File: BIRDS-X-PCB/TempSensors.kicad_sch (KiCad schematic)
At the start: 10 parts, among them U307 STDS75DS2F, U312 STDS75DS2F, U313 STDS75DS2F, U314 STDS75DS2F, U315 STDS75DS2F

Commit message: Prep docs for Rev5.1 release
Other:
- note added: "Note: Rev5 and Rev5.1 are missing I2C pull-up resistors. I2C pull-up resistors will be added in next rev."
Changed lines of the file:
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@@
   (paper "A4")
   (title_block
-    (rev "Rev5.0")
+    (date "2023-09-07")
+    (rev "Rev5.1")
   )
   (junction (at 92.71 78.74) (diameter 0) (color 0 0 0 0)
@@
     (effects (font (size 1.27 1.27)) (justify left bottom))
   )
+  (text "Note: Rev5 and Rev5.1 are missing I2C pull-up resistors.\nI2C pull-up resistors will be added in next rev."
+    (at 137.16 31.75 0)
+    (effects (font (size 1.27 1.27)) (justify left bottom))
+  )

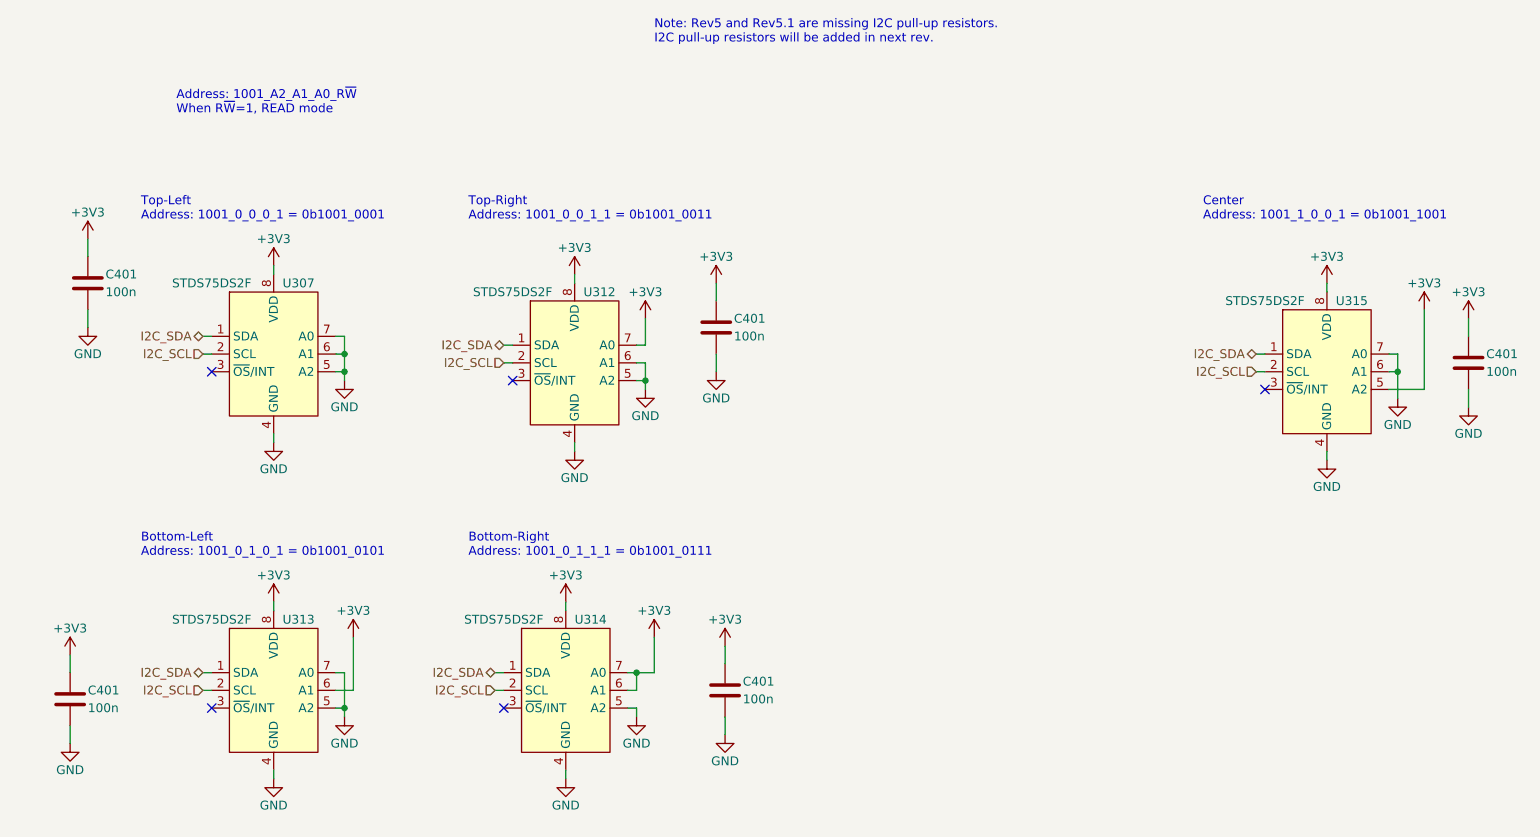
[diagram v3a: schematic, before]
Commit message: Update schematics with LinearCCDs, remove flash
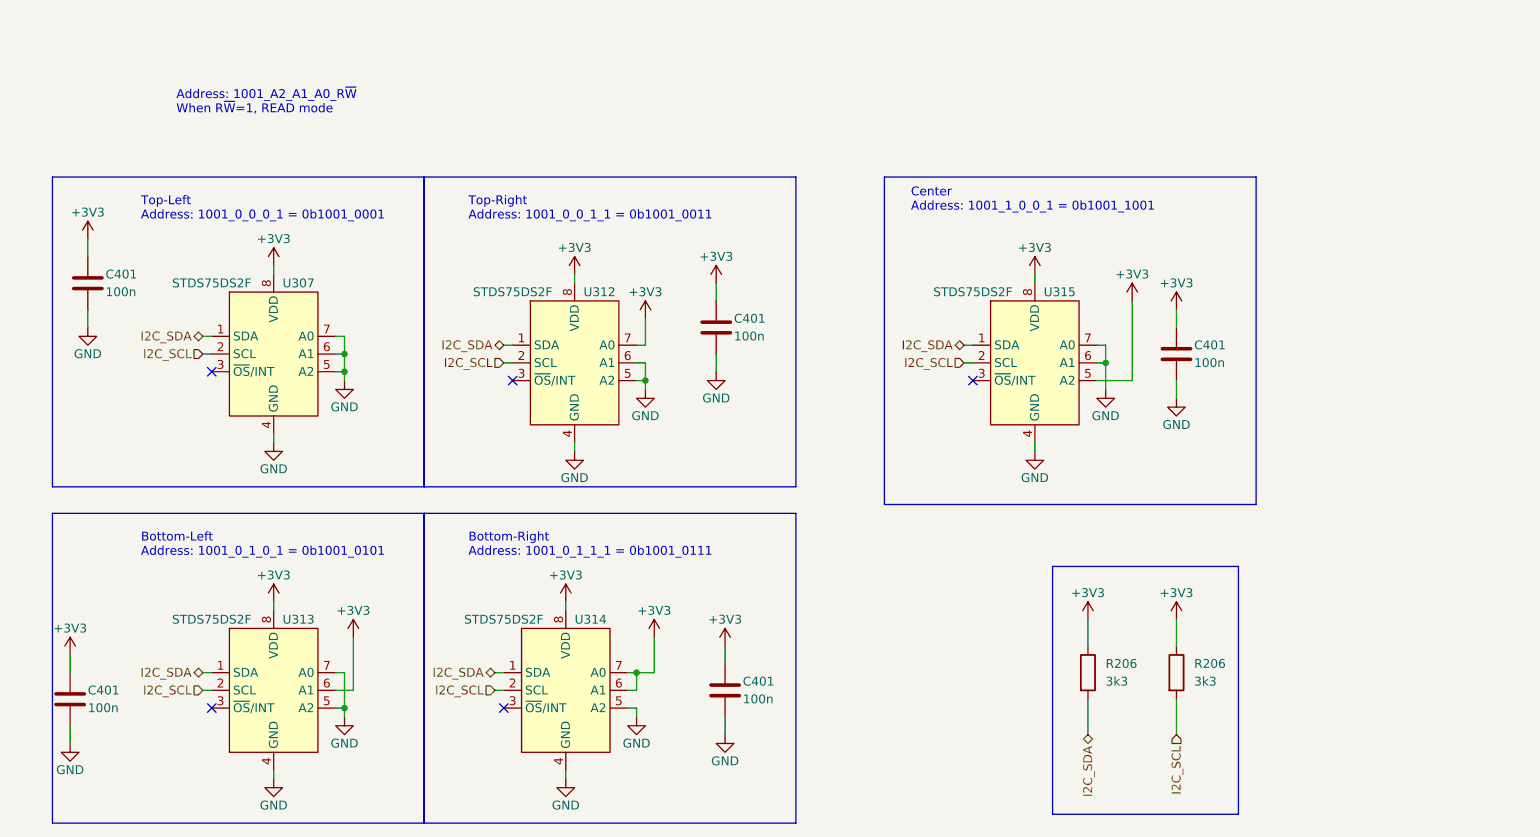
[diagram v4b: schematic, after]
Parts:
- added R206 (x2): 3k3, Resistor_SMD:R_0603_1608Metric_Pad0.98x0.95mm_HandSolder, symbol Device:R
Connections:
- net +3V3: now also R206.1, R206.1
- net I2C_SCL: now also R206.2
- net I2C_SDA: now also R206.2
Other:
- note removed: "Note: Rev5 and Rev5.1 are missing I2C pull-up resistors. I2C pull-up resistors will be added in next rev."
- moved on the sheet: C401, U315

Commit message: Schematic re-work (esp. RADFET fixes)
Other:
- note added: "I2C Pullups"
- moved on the sheet: C401, U307, U313
